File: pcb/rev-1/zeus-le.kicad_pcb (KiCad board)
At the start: 6 copper layers, 50 x 50 mm, 83 parts, among them J1 12402012E212A, J2 S2B-PH-SM4-TB, J3 B5B-PH-K-S, J4 BD125-10-A-0305-0580-L-B, J5 MSD-1-A, J6 B2B-PH-K-S, SW1 EVQPUD02K, U1 NUF2042XV6T1G, U10 D3V3F4U6S-7, U2 RT6160AWSC, U3 KTS1662EUW-TR, U4 BQ25150YFPR, U5 TLV320ADC6120IRTER, U6 WT02C40C-V3, U7 AP21510FM-7, U8 TPD6F003DQDR, U9 LP5810ADSDR

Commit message: pcb: rev-2: add missing 3D models, rev-1: update to KiCAD 9
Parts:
- U2: footprint zeus-le:Richtek_WLCSP-15_1.4x2.3mm_Layout3x5_P0.4mm_SMD -> zeus-le:Richtek_WLCSP-15_1.4x2.3mm_Layout3x5_P0.4mm_NSMD
- U3: footprint zeus-le:Kinetic_WLCSP-12_1.94x1.28mm_Layout4x3_P0.4mm_Ball0.25mm_Pad0.25mm_SMD -> zeus-le:Kinetic_WLCSP-12_1.94x1.28mm_Layout4x3_P0.4mm_Ball0.25mm_Pad0.25mm_NSMD
- U4: footprint zeus-le:Texas_DSBGA-20_1.615x2.015mm_Layout4x5_P0.4mm_SMD -> zeus-le:Texas_DSBGA-20_1.615x2.015mm_Layout4x5_P0.4mm_NSMD

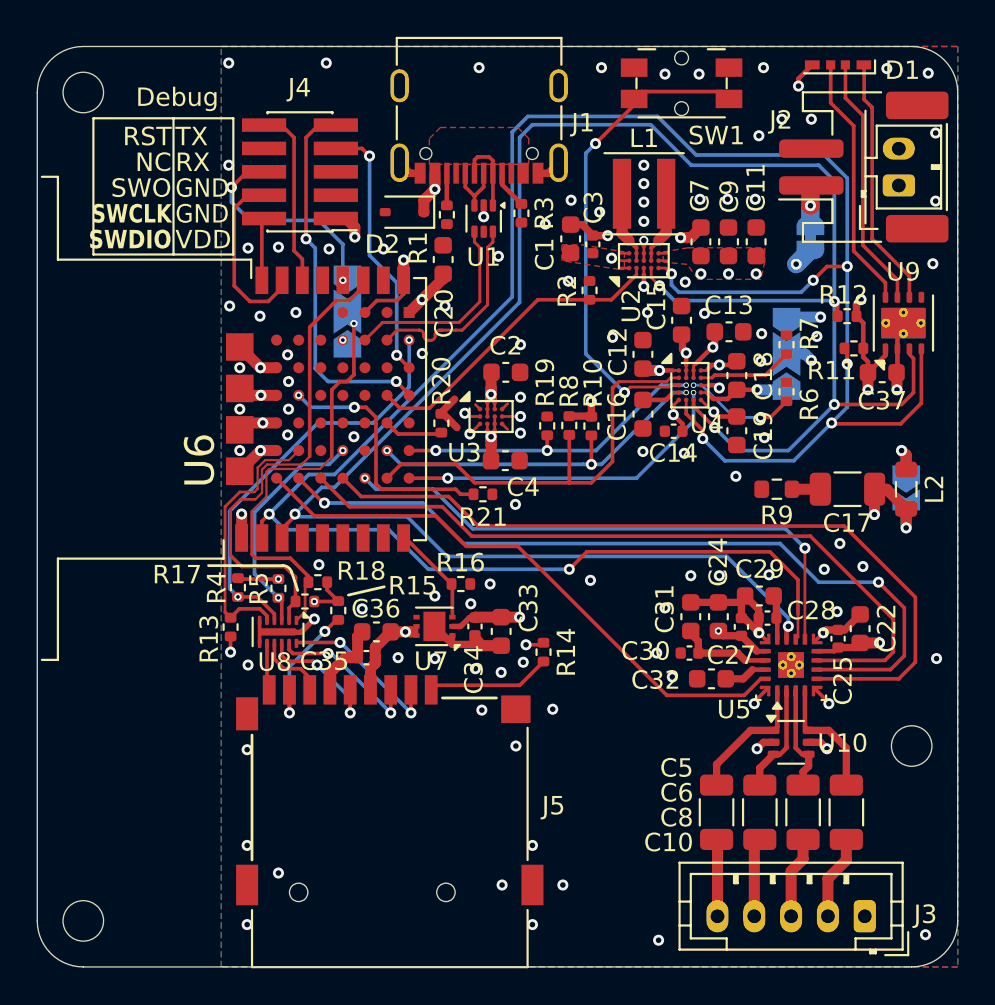
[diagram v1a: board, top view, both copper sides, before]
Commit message: Update PCBs
* Update to KiCad 10
* Update footprint for nRF53 module based on 1.01 datasheet with
  actually readable mechanical drawing
* Add 3D model for production nRF53 module
* Remove overlapping silkscreen on rev-1 with production nRF53 module
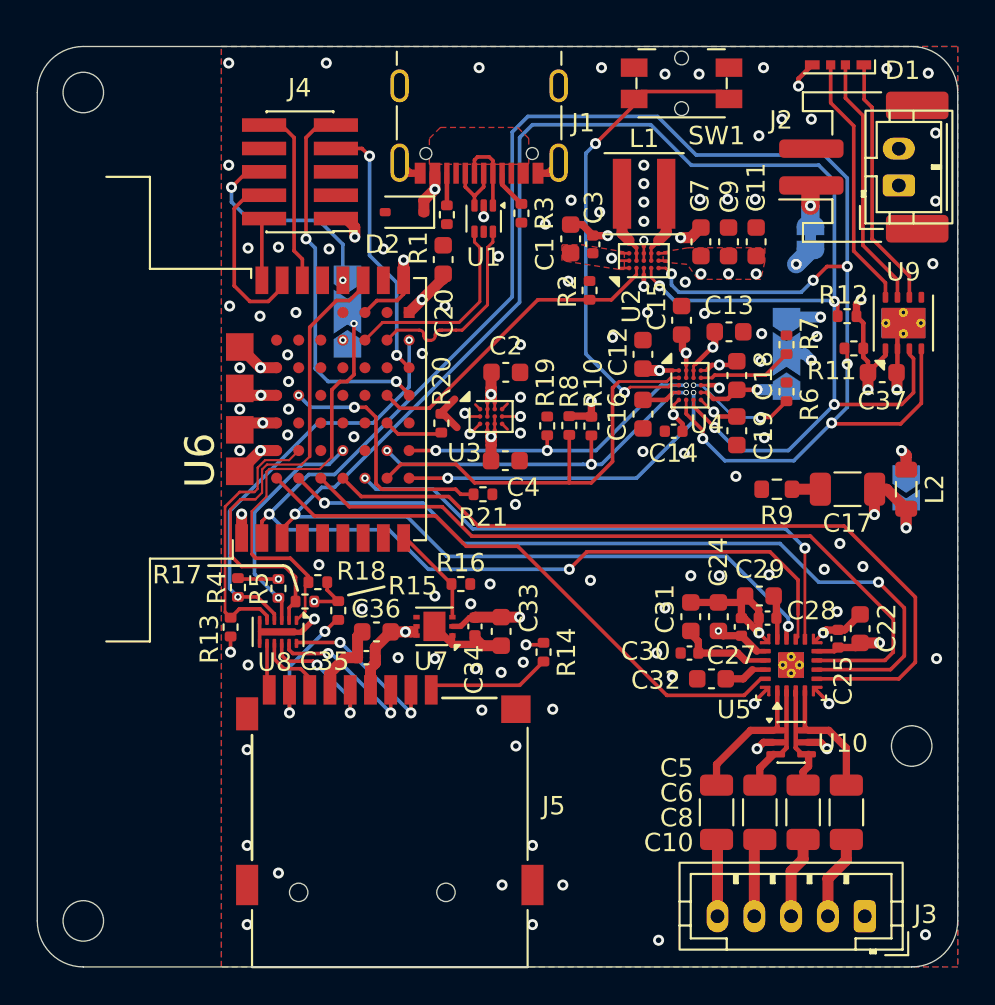
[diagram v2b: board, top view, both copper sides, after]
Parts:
- U6: value WT02C40C-V3 -> WT02C40C-VC; footprint zeus-le:WT02C40C -> zeus-le:WT02C40C-VC
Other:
- board text removed: "Debug"
- board text removed: "NC"
- board text removed: "RST"
- board text removed: "RX"
- board text removed: "SWCLK"
- board text removed: "SWDIO"
- board text removed: "SWO"
- board text removed: "TX"
- board text removed: "VDD"
